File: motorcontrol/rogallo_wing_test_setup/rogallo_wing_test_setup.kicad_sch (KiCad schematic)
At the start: 18 parts

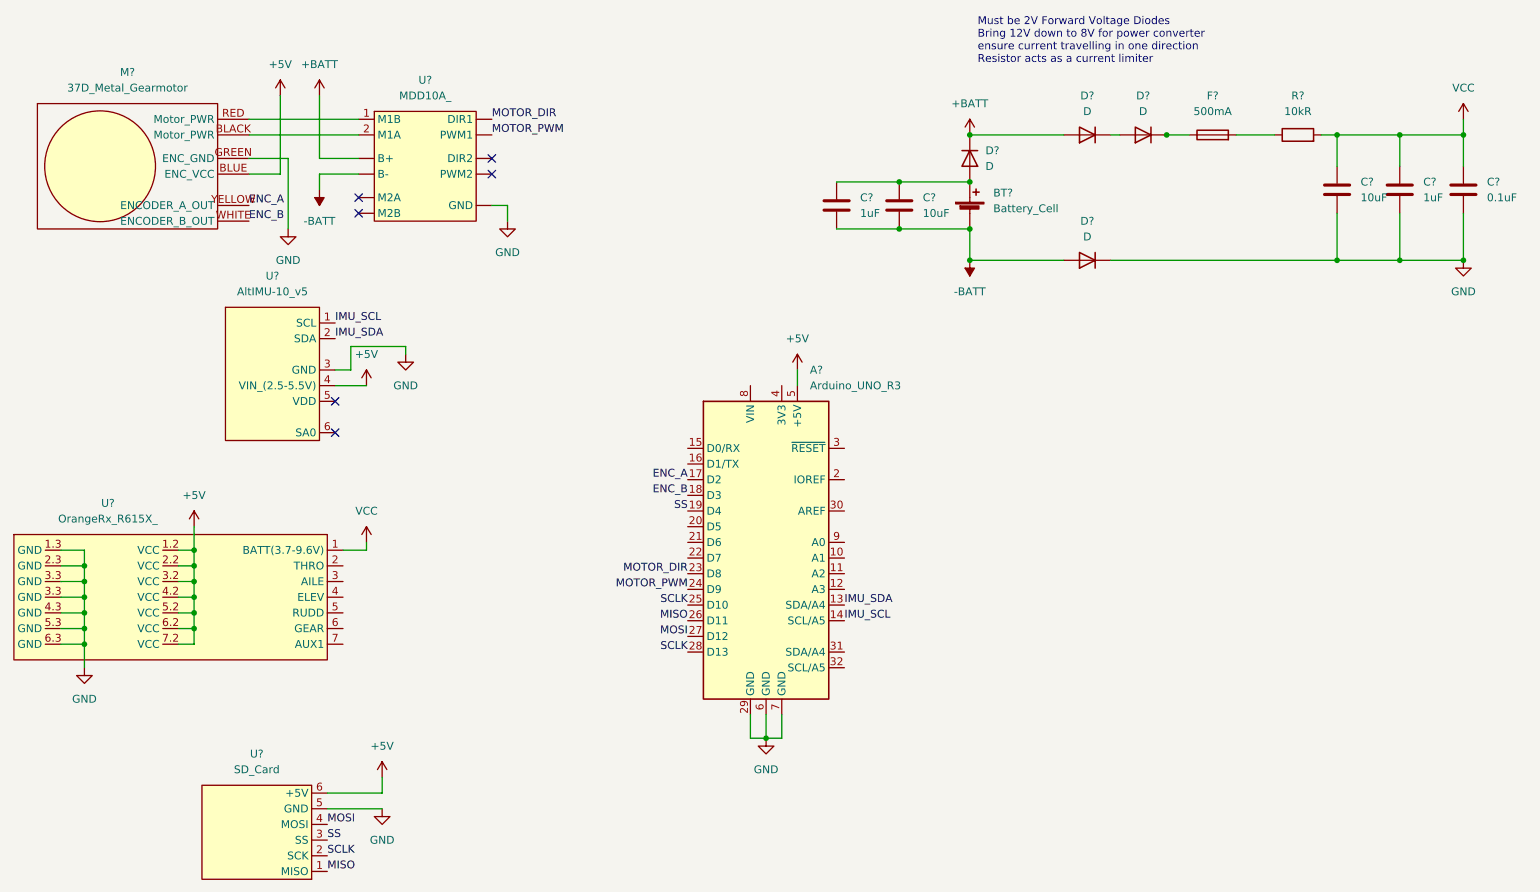
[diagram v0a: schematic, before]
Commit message: swapped for arduino nano
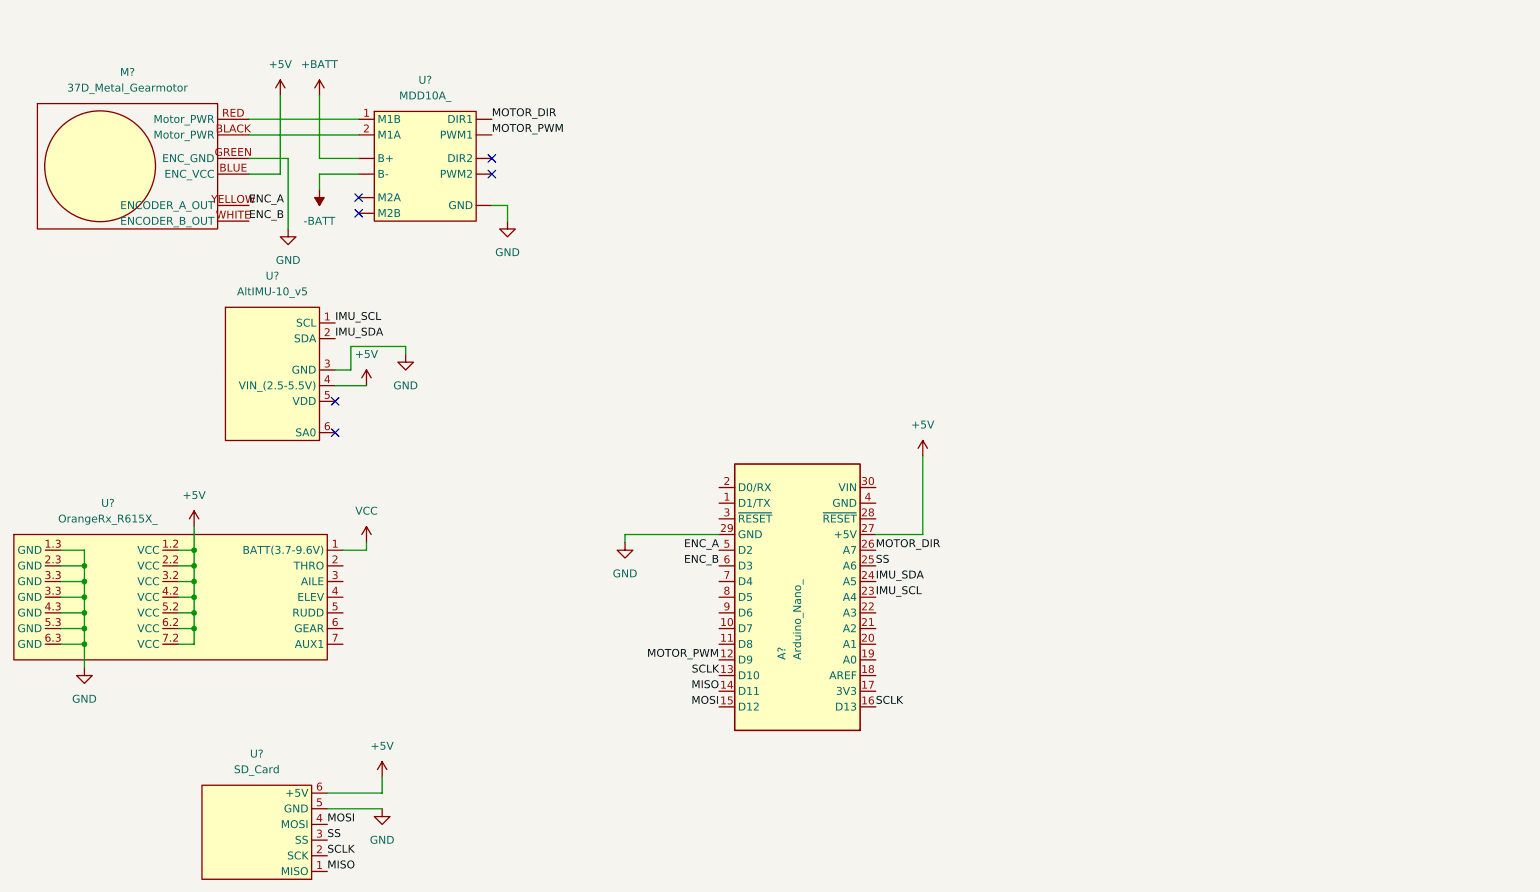
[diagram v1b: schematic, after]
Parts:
- removed A?: Arduino_UNO_R3, Module:Arduino_UNO_R3, symbol MCU_Module:Arduino_UNO_R3
- removed BT?: Battery_Cell, symbol Device:Battery_Cell
- removed C?: 0.1uF, symbol Device:C
- removed C? (x2): 10uF, symbol Device:C
- removed C? (x2): 1uF, symbol Device:C
- removed D? (x4): D, symbol Device:D
- removed F?: 500mA, symbol Device:Fuse
- removed R?: 10kR, symbol Device:R
- added A?: Arduino_Nano_, Module:Arduino_Nano, symbol MCU_Module:Arduino_Nano_v3.x
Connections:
- net +5V: now also A?.27 (+5V)
- net ENC_A: now also A?.5 (D2)
- net ENC_B: now also A?.6 (D3)
- net GND: now also A?.29 (GND)
- net IMU_SCL: now also A?.23 (A4)
- net IMU_SDA: now also A?.24 (A5)
- net MISO: now also A?.14 (D11)
- net MOSI: now also A?.15 (D12)
- net MOTOR_DIR: now also A?.26 (A7)
- net MOTOR_PWM: now also A?.12 (D9)
- net SCLK: now also A?.13 (D10), A?.16 (D13)
- net SS: now also A?.25 (A6)
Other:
- note removed: "Must be 2V Forward Voltage Diodes Bring 12V down to 8V for power converter ensure current travelling in one direction Resistor acts as a current limiter"
